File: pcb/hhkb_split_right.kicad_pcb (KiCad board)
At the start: 2 copper layers, 173.7 x 97.4 mm, 92 parts, among them SW1 6, SW10 Y, SW11 U, SW12 I, SW13 O, SW14 P, SW15 [, SW16 ], SW17 Del, SW18 H, SW19 J, SW2 7, SW20 K, SW21 L, SW22 ;, SW23 ', SW24 Enter, SW25 N, SW26 M, SW27 ,, SW28 ., SW29 /, SW3 8, SW30 Shift, SW31 Fn, SW32 R-Space, SW33 Meta, SW34 Alt, SW4 9, SW5 0, SW6 -, SW7 =, SW8 \, SW9 `, U1 74LVC595, U2 74LVC595

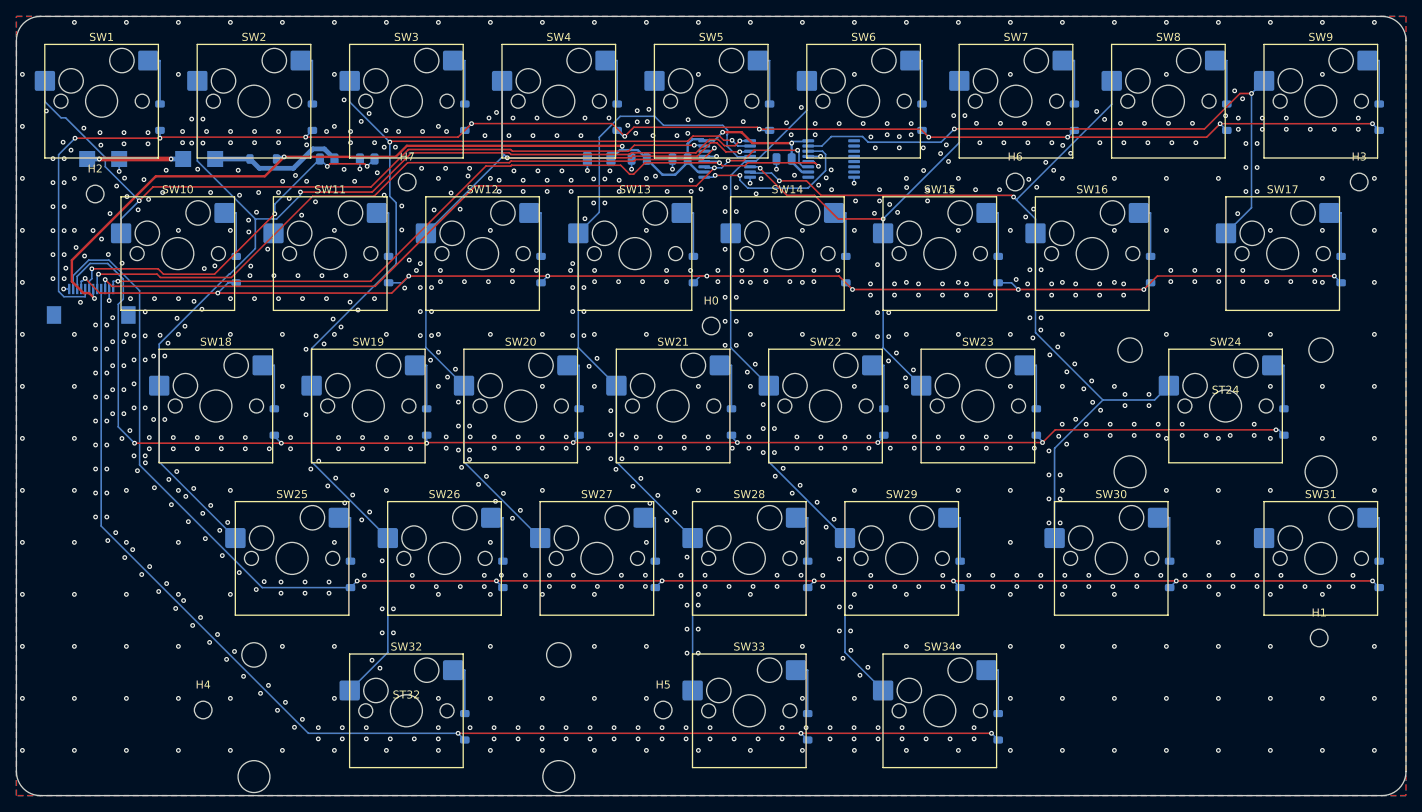
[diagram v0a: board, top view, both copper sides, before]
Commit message: 右基板 COL8/V3V3 の未配線を中継ビアで解消した
Freerouting が SW17-SW31 間（COL8）を毎回配線し損ねていた。
部分配線を見ると、SW17 から南（SW31 方向）への探索を一度も
試みず、北の混雑領域へ迷い込んで力尽きていた——基板の物理的な
制約ではなく、探索ヒューリスティックが局所解にはまったもの。

2点間の中間に同じネットのビアを1個置き、Freeroutingにとって
「近距離問題2つ」に分割することで解決（実測5回連続成功）。

副作用があった。COL8側にビアを足すと、無関係なはずのV3V3
（D_PWR→J_DB、パッド幅0.30mmで元々ギリギリ）が5回連続で
未配線になった。Freerouting内部の配線順序が変わり、際どい
ネットにしわ寄せが行っただけと判断し、V3V3側にも中継ビアを
足して両立させた（2回連続成功で確認）。

右基板専用（左基板ではこの詰まりが起きていない）。

確認: DRC 左右とも違反0・未配線0（実測、ハッシュ一致）。
pytest tools/test_pcb.py -k drc 6件全通過。
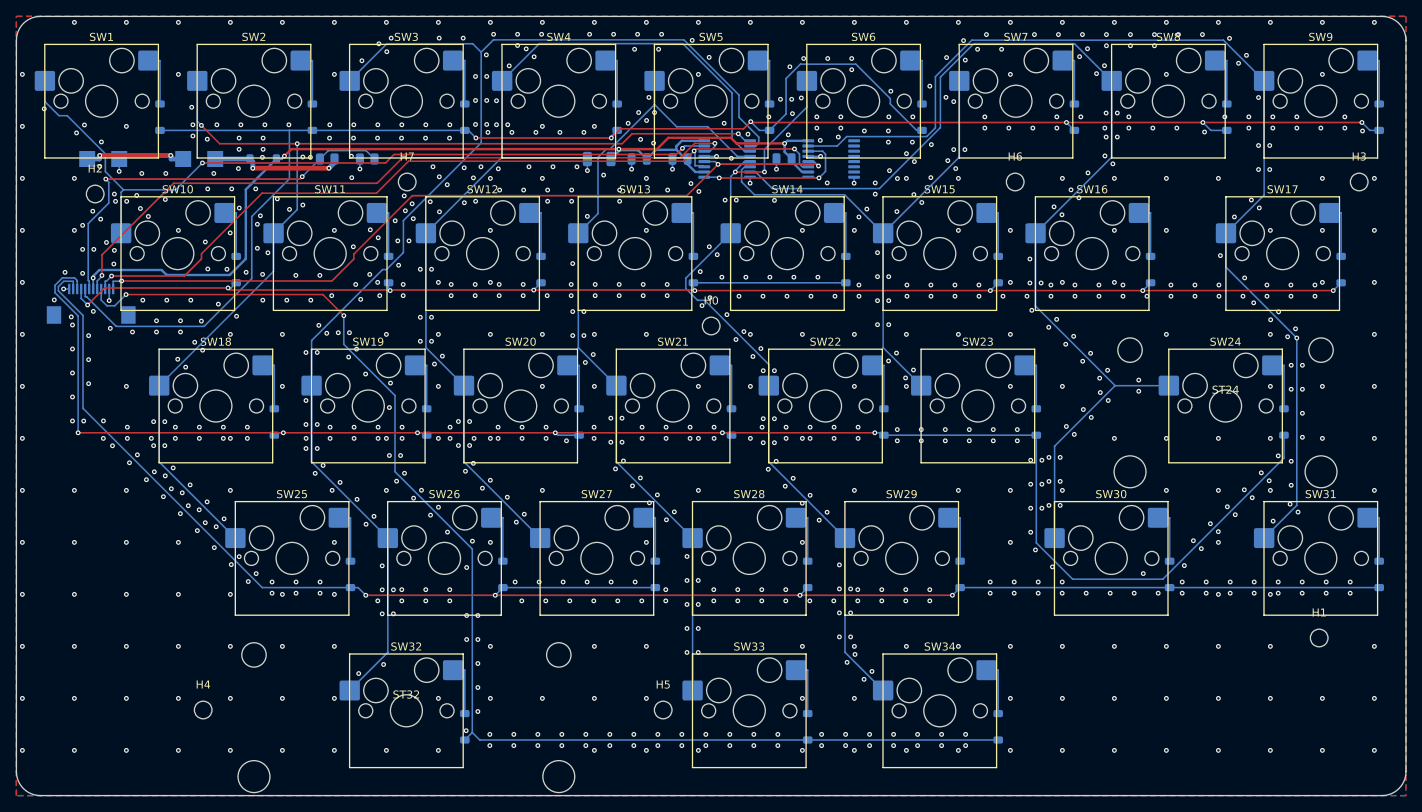
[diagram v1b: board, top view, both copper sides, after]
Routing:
- net COL8: track 79.7 -> 132.8 mm, vias 2 -> 1
- net ROW0: track 200.6 -> 238.1 mm, vias 10 -> 6
- net ROW2: track 182.4 -> 206.2 mm, vias 8 -> 6
- net COL2: track 134.8 -> 157.5 mm, vias 2 -> 0
- net COL7: track 112.8 -> 134.3 mm, vias 2 -> 0
- net ROW3: track 202.0 -> 213.5 mm, vias 7 -> 4
- net ROW1: track 176.1 -> 187.0 mm, vias 9 -> 8
- net COL3: track 99.4 -> 108.9 mm, vias 2 -> 0
- net COL5: track 88.8 -> 97.8 mm, vias 0 -> 2
- net V3V3: track 122.4 -> 128.4 mm, vias 5 -> 4
- net ROW4: track 155.2 -> 159.9 mm, vias 3 -> 2
- net VBATT_SENSE: track 46.0 -> 50.5 mm, vias 4 -> 2
- net COL6: track 63.4 -> 67.1 mm, vias 2 -> 0
- net COL4: track 103.9 -> 101.0 mm
- net SPI_MOSI: track 87.2 -> 88.8 mm
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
